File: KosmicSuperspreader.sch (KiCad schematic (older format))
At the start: 5 parts

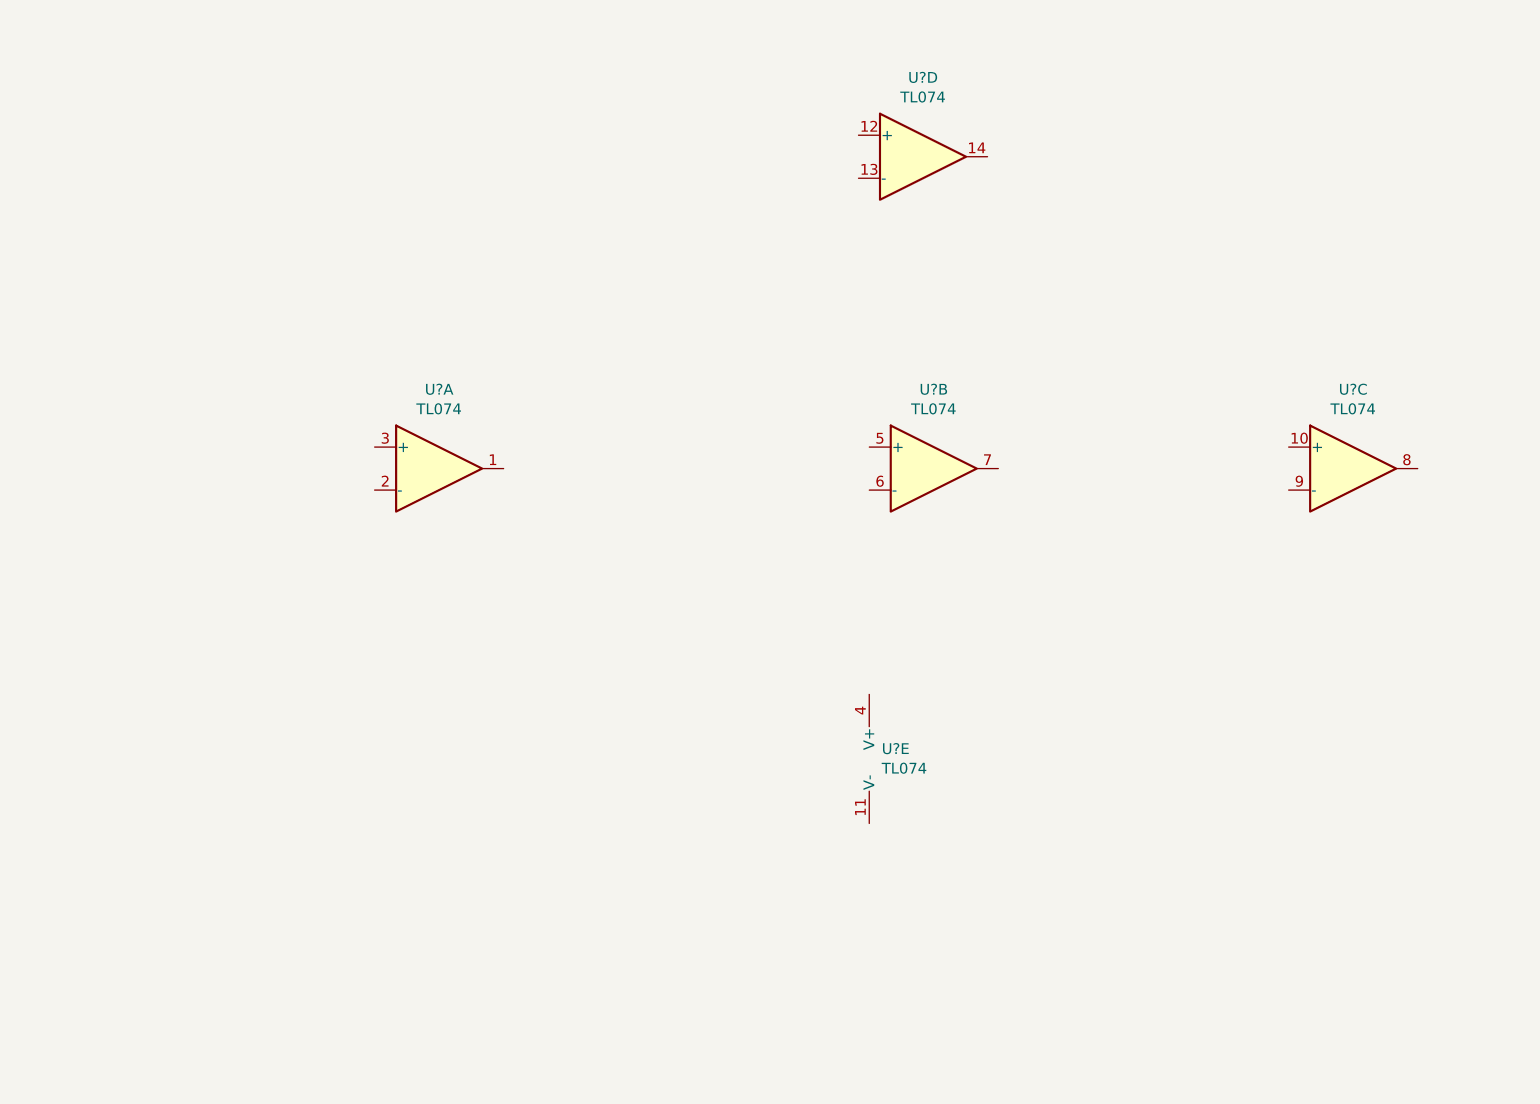
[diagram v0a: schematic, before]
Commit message: Add resistors
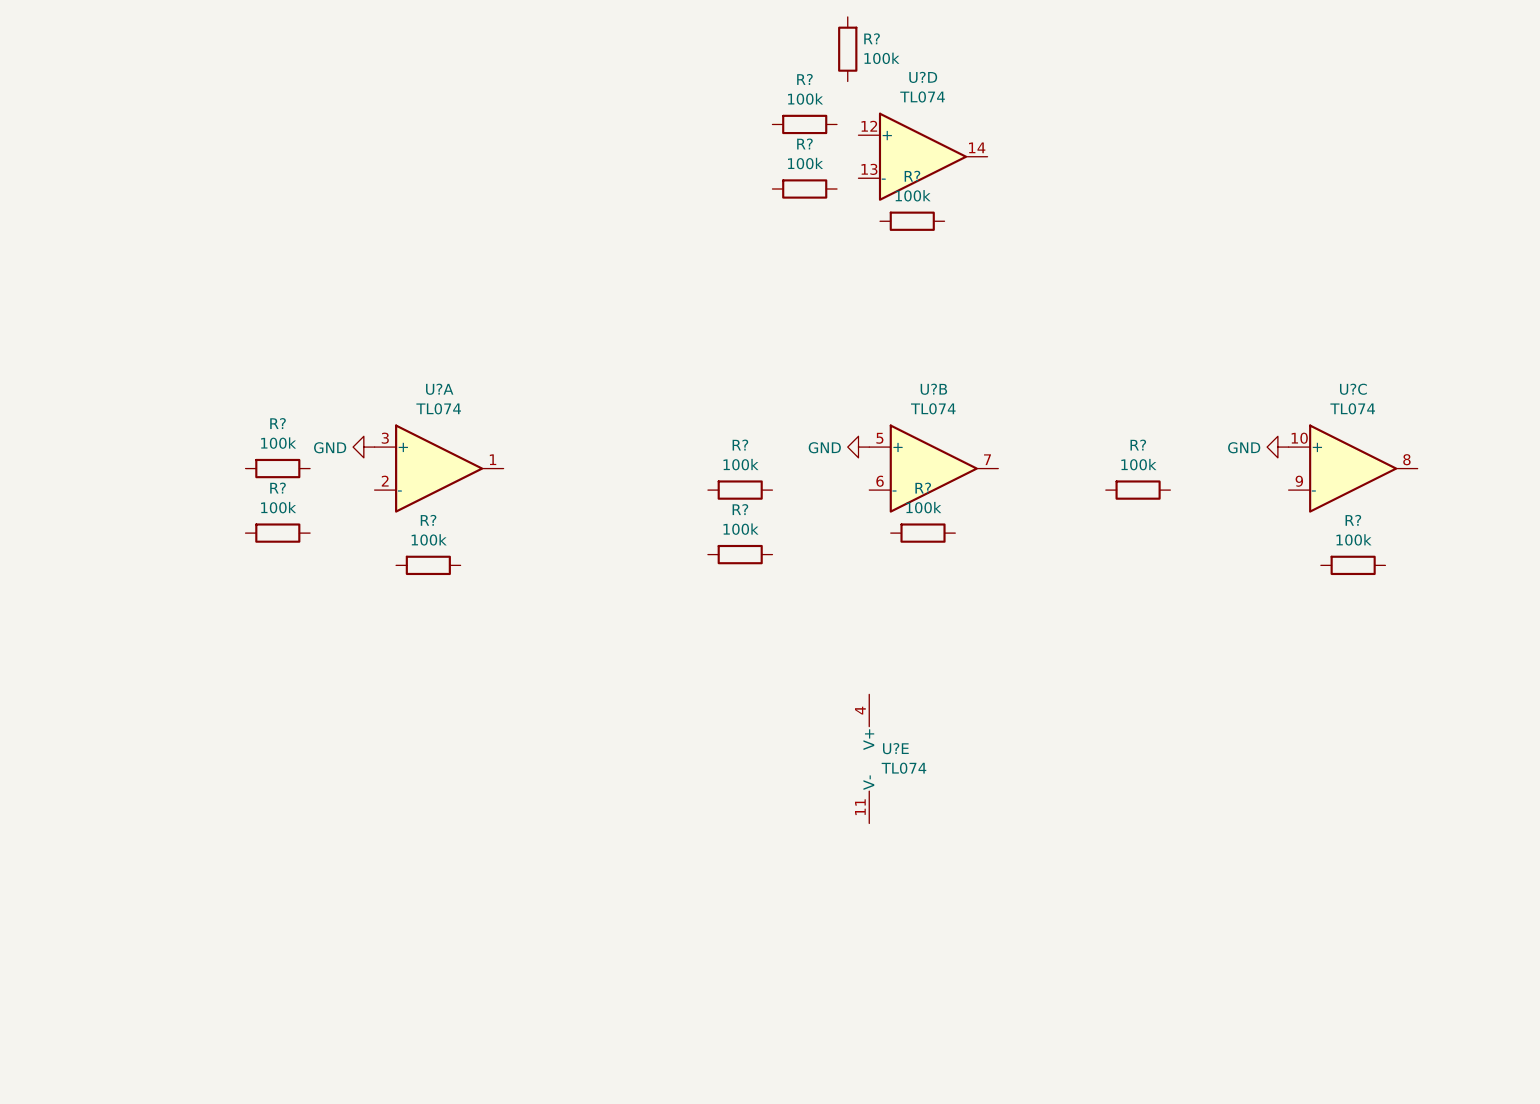
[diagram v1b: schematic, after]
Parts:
- added R? (x12): 100k, symbol Device:R
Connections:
- net GND: now reaches U?.3 (+)
- net GND: now also U?.10 (+), U?.5 (+)
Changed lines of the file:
@@
 	1    0    0    -1
 $EndComp
+$Comp
+L power:GND #PWR?
+U 1 1 60B1F41E
+P 2700 3900
+F 0 "#PWR?" H 2700 3650 50  0001 C CNN
+F 1 "GND" V 2705 3772 50  0000 R CNN
+F 2 "" H 2700 3900 50  0001 C CNN
+F 3 "" H 2700 3900 50  0001 C CNN
+	1    2700 3900
+	0    1    1    0
+$EndComp
+$Comp
+L power:GND #PWR?
+U 1 1 60B1F83E
+P 5000 3900
+F 0 "#PWR?" H 5000 3650 50  0001 C CNN
+F 1 "GND" V 5005 3772 50  0000 R CNN
+F 2 "" H 5000 3900 50  0001 C CNN
+F 3 "" H 5000 3900 50  0001 C CNN
+	1    5000 3900
+	0    1    1    0
+$EndComp
+$Comp
+L power:GND #PWR?
+U 1 1 60B1FCAA
+P 6950 3900
+F 0 "#PWR?" H 6950 3650 50  0001 C CNN
+F 1 "GND" V 6955 3772 50  0000 R CNN
+F 2 "" H 6950 3900 50  0001 C CNN
+F 3 "" H 6950 3900 50  0001 C CNN
+	1    6950 3900
+	0    1    1    0
+$EndComp
+$Comp
+L Device:R R?
+U 1 1 60B211E0
+P 5200 2850
+F 0 "R?" V 4993 2850 50  0000 C CNN
+F 1 "100k" V 5084 2850 50  0000 C CNN
+F 2 "" V 5130 2850 50  0001 C CNN
+F 3 "~" H 5200 2850 50  0001 C CNN
+F 4 "A-2248" V 5200 2850 50  0001 C CNN "Part"
+	1    5200 2850
+	0    1    1    0
+$EndComp
+$Comp
+L Device:R R?
+U 1 1 60B214C6
+P 5250 4300
+F 0 "R?" V 5043 4300 50  0000 C CNN
+F 1 "100k" V 5134 4300 50  0000 C CNN
+F 2 "" V 5180 4300 50  0001 C CNN
+F 3 "~" H 5250 4300 50  0001 C CNN
+F 4 "A-2248" V 5250 4300 50  0001 C CNN "Part"
+	1    5250 4300
+	0    1    1    0
+$EndComp
+$Comp
+L Device:R R?
+U 1 1 60B21E94
+P 4400 4100
+F 0 "R?" V 4193 4100 50  0000 C CNN
+F 1 "100k" V 4284 4100 50  0000 C CNN
+F 2 "" V 4330 4100 50  0001 C CNN
+F 3 "~" H 4400 4100 50  0001 C CNN
+F 4 "A-2248" V 4400 4100 50  0001 C CNN "Part"
+	1    4400 4100
+	0    1    1    0
+$EndComp
+$Comp
+L Device:R R?
+U 1 1 60B22499
+P 4400 4400
+F 0 "R?" V 4193 4400 50  0000 C CNN
+F 1 "100k" V 4284 4400 50  0000 C CNN
+F 2 "" V 4330 4400 50  0001 C CNN
+F 3 "~" H 4400 4400 50  0001 C CNN
+F 4 "A-2248" V 4400 4400 50  0001 C CNN "Part"
+	1    4400 4400
+	0    1    1    0
+$EndComp
+$Comp
+L Device:R R?
+U 1 1 60B2276E
+P 4700 2400
+F 0 "R?" V 4493 2400 50  0000 C CNN
+F 1 "100k" V 4584 2400 50  0000 C CNN
+F 2 "" V 4630 2400 50  0001 C CNN
+F 3 "~" H 4700 2400 50  0001 C CNN
+F 4 "A-2248" V 4700 2400 50  0001 C CNN "Part"
+	1    4700 2400
+	0    1    1    0
+$EndComp
+$Comp
+L Device:R R?
+U 1 1 60B22DB5
+P 4700 2700
+F 0 "R?" V 4493 2700 50  0000 C CNN
+F 1 "100k" V 4584 2700 50  0000 C CNN
+F 2 "" V 4630 2700 50  0001 C CNN
+F 3 "~" H 4700 2700 50  0001 C CNN
+F 4 "A-2248" V 4700 2700 50  0001 C CNN "Part"
+	1    4700 2700
+	0    1    1    0
+$EndComp
+$Comp
+L Device:R R?
+U 1 1 60B23C3D
+P 4900 2050
+F 0 "R?" H 4830 2004 50  0000 R CNN
+F 1 "100k" H 4830 2095 50  0000 R CNN
+F 2 "" V 4830 2050 50  0001 C CNN
+F 3 "~" H 4900 2050 50  0001 C CNN
+F 4 "A-2248" V 4900 2050 50  0001 C CNN "Part"
+	1    4900 2050
+	-1   0    0    1
+$EndComp
+$Comp
+L Device:R R?
+U 1 1 60B242ED
+P 6250 4100
+F 0 "R?" V 6043 4100 50  0000 C CNN
+F 1 "100k" V 6134 4100 50  0000 C CNN
+F 2 "" V 6180 4100 50  0001 C CNN
+F 3 "~" H 6250 4100 50  0001 C CNN
+F 4 "A-2248" V 6250 4100 50  0001 C CNN "Part"
+	1    6250 4100
+	0    1    1    0
+$EndComp
+$Comp
+L Device:R R?
+U 1 1 60B24980
+P 7250 4450
+F 0 "R?" V 7043 4450 50  0000 C CNN
+F 1 "100k" V 7134 4450 50  0000 C CNN
+F 2 "" V 7180 4450 50  0001 C CNN
+F 3 "~" H 7250 4450 50  0001 C CNN
+F 4 "A-2248" V 7250 4450 50  0001 C CNN "Part"
+	1    7250 4450
+	0    1    1    0
+$EndComp
+$Comp
+L Device:R R?
+U 1 1 60B24D1D
+P 2950 4450
+F 0 "R?" V 2743 4450 50  0000 C CNN
+F 1 "100k" V 2834 4450 50  0000 C CNN
+F 2 "" V 2880 4450 50  0001 C CNN
+F 3 "~" H 2950 4450 50  0001 C CNN
+F 4 "A-2248" V 2950 4450 50  0001 C CNN "Part"
+	1    2950 4450
+	0    1    1    0
+$EndComp
+$Comp
+L Device:R R?
+U 1 1 60B25284
+P 2250 4300
+F 0 "R?" V 2043 4300 50  0000 C CNN
+F 1 "100k" V 2134 4300 50  0000 C CNN
+F 2 "" V 2180 4300 50  0001 C CNN
+F 3 "~" H 2250 4300 50  0001 C CNN
+F 4 "A-2248" V 2250 4300 50  0001 C CNN "Part"
+	1    2250 4300
+	0    1    1    0
+$EndComp
+$Comp
+L Device:R R?
+U 1 1 60B25ADF
+P 2250 4000
+F 0 "R?" V 2043 4000 50  0000 C CNN
+F 1 "100k" V 2134 4000 50  0000 C CNN
+F 2 "" V 2180 4000 50  0001 C CNN
+F 3 "~" H 2250 4000 50  0001 C CNN
+F 4 "A-2248" V 2250 4000 50  0001 C CNN "Part"
+	1    2250 4000
+	0    1    1    0
+$EndComp
 $EndSCHEMATC

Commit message: wires
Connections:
- net GND: now also R?.2
- net at U?.1: now also R?.1
- net at U?.2 (-): now also R?.1, R?.1, R?.2
- net at U?.6 (-): now also R?.1, R?.1, R?.2
- net at U?.7: now also R?.1, R?.2
- net at U?.8: now also R?.1
- net at U?.9 (-): now also R?.1, R?.2
- net at U?.12 (+): now also R?.1, R?.1
- net at U?.13 (-): now also R?.1, R?.2
- net at U?.14: now also R?.1
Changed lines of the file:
@@
 	0    1    1    0
 $EndComp
+Wire Wire Line
+	2400 4000 2400 4100
+Wire Wire Line
+	2700 4100 2400 4100
+Connection ~ 2400 4100
+Wire Wire Line
+	2400 4100 2400 4300
+Wire Wire Line
+	2800 4450 2700 4450
+Wire Wire Line
+	2700 4450 2700 4100
+Connection ~ 2700 4100
+Wire Wire Line
+	3100 4450 3300 4450
+Wire Wire Line
+	3300 4450 3300 4000
+Wire Wire Line
+	4550 4100 4550 4400
+Wire Wire Line
+	5000 4100 4550 4100
+Connection ~ 4550 4100
+Wire Wire Line
+	5100 4300 5000 4300
+Wire Wire Line
+	5000 4300 5000 4100
+Connection ~ 5000 4100
+Wire Wire Line
+	5400 4300 5600 4300
+Wire Wire Line
+	5600 4300 5600 4100
+Wire Wire Line
+	6400 4100 6950 4100
+Wire Wire Line
+	6100 4100 5600 4100
+Connection ~ 5600 4100
+Wire Wire Line
+	5600 4100 5600 4000
+Wire Wire Line
+	7100 4450 6950 4450
+Wire Wire Line
+	6950 4450 6950 4100
+Connection ~ 6950 4100
+Wire Wire Line
+	7550 4000 7550 4450
+Wire Wire Line
+	7550 4450 7400 4450
+Wire Wire Line
+	4850 2700 4950 2700
+Wire Wire Line
+	4950 2700 4950 2650
+Wire Wire Line
+	4850 2400 4900 2400
+Wire Wire Line
+	4950 2400 4950 2450
+Wire Wire Line
+	5350 2850 5550 2850
+Wire Wire Line
+	5550 2850 5550 2550
+Wire Wire Line
+	5050 2850 4950 2850
+Wire Wire Line
+	4950 2850 4950 2700
+Connection ~ 4950 2700
+Wire Wire Line
+	4900 2200 4900 2400
+Connection ~ 4900 2400
+Wire Wire Line
+	4900 2400 4950 2400
+$Comp
+L power:GND #PWR?
+U 1 1 60B2A62B
+P 5400 1900
+F 0 "#PWR?" H 5400 1650 50  0001 C CNN
+F 1 "GND" H 5405 1727 50  0000 C CNN
+F 2 "" H 5400 1900 50  0001 C CNN
+F 3 "" H 5400 1900 50  0001 C CNN
+	1    5400 1900
+	1    0    0    -1
+$EndComp
+Wire Wire Line
+	4900 1900 5400 1900
 $EndSCHEMATC

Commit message: Jacks
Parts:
- added J? (x5): AudioJack2_Ground_Switch, symbol Connector:AudioJack2_Ground_Switch
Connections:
- net GND: now also J?.G, J?.G, J?.G, J?.G, J?.G
- net at R?.1, U?.1: now also R?.2, R?.2
- net at R?.2: now also R?.2
- no-connect marks 0 -> 15
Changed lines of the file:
@@
 	3100 4450 3300 4450
-Wire Wire Line
-	3300 4450 3300 4000
 Wire Wire Line
 	4550 4100 4550 4400
@@
 Wire Wire Line
 	4900 1900 5400 1900
+Wire Wire Line
+	3300 4100 3400 4100
+Wire Wire Line
+	3300 4000 3300 4100
+Connection ~ 3300 4100
+Wire Wire Line
+	3300 4100 3300 4450
+Wire Wire Line
+	3400 4100 3400 2700
+Wire Wire Line
+	3400 2700 4550 2700
+Connection ~ 3400 4100
+Wire Wire Line
+	3400 4100 4250 4100
+Wire Wire Line
+	4250 4400 4000 4400
+Wire Wire Line
+	4000 4400 4000 2400
+Wire Wire Line
+	4000 2400 4550 2400
+$Comp
+L Connector:AudioJack2_Ground_Switch J?
+U 1 1 60B2E747
+P 2200 6350
+F 0 "J?" H 2232 6775 50  0000 C CNN
+F 1 "AudioJack2_Ground_Switch" H 2232 6684 50  0000 C CNN
+F 2 "" H 2200 6550 50  0001 C CNN
+F 3 "~" H 2200 6550 50  0001 C CNN
+F 4 "A-1121" H 2200 6350 50  0001 C CNN "Part"
+	1    2200 6350
+	1    0    0    -1
+$EndComp
+NoConn ~ 2400 6450
+NoConn ~ 2400 6250
+NoConn ~ 2400 6150
+$Comp
+L power:GND #PWR?
+U 1 1 60B30BB2
+P 2200 6650
+F 0 "#PWR?" H 2200 6400 50  0001 C CNN
+F 1 "GND" H 2205 6477 50  0000 C CNN
+F 2 "" H 2200 6650 50  0001 C CNN
+F 3 "" H 2200 6650 50  0001 C CNN
+	1    2200 6650
+	1    0    0    -1
+$EndComp
+$Comp
+L Connector:AudioJack2_Ground_Switch J?
+U 1 1 60B31450
+P 2900 6350
+F 0 "J?" H 2932 6775 50  0000 C CNN
+F 1 "AudioJack2_Ground_Switch" H 2932 6684 50  0000 C CNN
+F 2 "" H 2900 6550 50  0001 C CNN
+F 3 "~" H 2900 6550 50  0001 C CNN
+F 4 "A-1121" H 2900 6350 50  0001 C CNN "Part"
+	1    2900 6350
+	1    0    0    -1
+$EndComp
+NoConn ~ 3100 6450
+NoConn ~ 3100 6250
+NoConn ~ 3100 6150
+$Comp
+L power:GND #PWR?
+U 1 1 60B31769
+P 2900 6650
+F 0 "#PWR?" H 2900 6400 50  0001 C CNN
+F 1 "GND" H 2905 6477 50  0000 C CNN
+F 2 "" H 2900 6650 50  0001 C CNN
+F 3 "" H 2900 6650 50  0001 C CNN
+	1    2900 6650
+	1    0    0    -1
+$EndComp
+$Comp
+L Connector:AudioJack2_Ground_Switch J?
+U 1 1 60B33779
+P 3550 6350
+F 0 "J?" H 3582 6775 50  0000 C CNN
+F 1 "AudioJack2_Ground_Switch" H 3582 6684 50  0000 C CNN
+F 2 "" H 3550 6550 50  0001 C CNN
+F 3 "~" H 3550 6550 50  0001 C CNN
+F 4 "A-1121" H 3550 6350 50  0001 C CNN "Part"
+	1    3550 6350
+	1    0    0    -1
+$EndComp
+NoConn ~ 3750 6450
+NoConn ~ 3750 6250
+NoConn ~ 3750 6150
+$Comp
+L power:GND #PWR?
+U 1 1 60B33AC2
+P 3550 6650
+F 0 "#PWR?" H 3550 6400 50  0001 C CNN
+F 1 "GND" H 3555 6477 50  0000 C CNN
+F 2 "" H 3550 6650 50  0001 C CNN
+F 3 "" H 3550 6650 50  0001 C CNN
+	1    3550 6650
+	1    0    0    -1
+$EndComp
+$Comp
+L Connector:AudioJack2_Ground_Switch J?
+U 1 1 60B33ACD
+P 4250 6350
+F 0 "J?" H 4282 6775 50  0000 C CNN
+F 1 "AudioJack2_Ground_Switch" H 4282 6684 50  0000 C CNN
+F 2 "" H 4250 6550 50  0001 C CNN
+F 3 "~" H 4250 6550 50  0001 C CNN
+F 4 "A-1121" H 4250 6350 50  0001 C CNN "Part"
+	1    4250 6350
+	1    0    0    -1
+$EndComp
+NoConn ~ 4450 6450
+NoConn ~ 4450 6250
+NoConn ~ 4450 6150
+$Comp
+L power:GND #PWR?
+U 1 1 60B33ADA
+P 4250 6650
+F 0 "#PWR?" H 4250 6400 50  0001 C CNN
+F 1 "GND" H 4255 6477 50  0000 C CNN
+F 2 "" H 4250 6650 50  0001 C CNN
+F 3 "" H 4250 6650 50  0001 C CNN
+	1    4250 6650
+	1    0    0    -1
+$EndComp
+$Comp
+L Connector:AudioJack2_Ground_Switch J?
+U 1 1 60B3629C
+P 1600 6350
+F 0 "J?" H 1632 6775 50  0000 C CNN
+F 1 "AudioJack2_Ground_Switch" H 1632 6684 50  0000 C CNN
+F 2 "" H 1600 6550 50  0001 C CNN
+F 3 "~" H 1600 6550 50  0001 C CNN
+F 4 "A-1121" H 1600 6350 50  0001 C CNN "Part"
+	1    1600 6350
+	1    0    0    -1
+$EndComp
+NoConn ~ 1800 6450
+NoConn ~ 1800 6250
+NoConn ~ 1800 6150
+$Comp
+L power:GND #PWR?
+U 1 1 60B36645
+P 1600 6650
+F 0 "#PWR?" H 1600 6400 50  0001 C CNN
+F 1 "GND" H 1605 6477 50  0000 C CNN
+F 2 "" H 1600 6650 50  0001 C CNN
+F 3 "" H 1600 6650 50  0001 C CNN
+	1    1600 6650
+	1    0    0    -1
+$EndComp
 $EndSCHEMATC

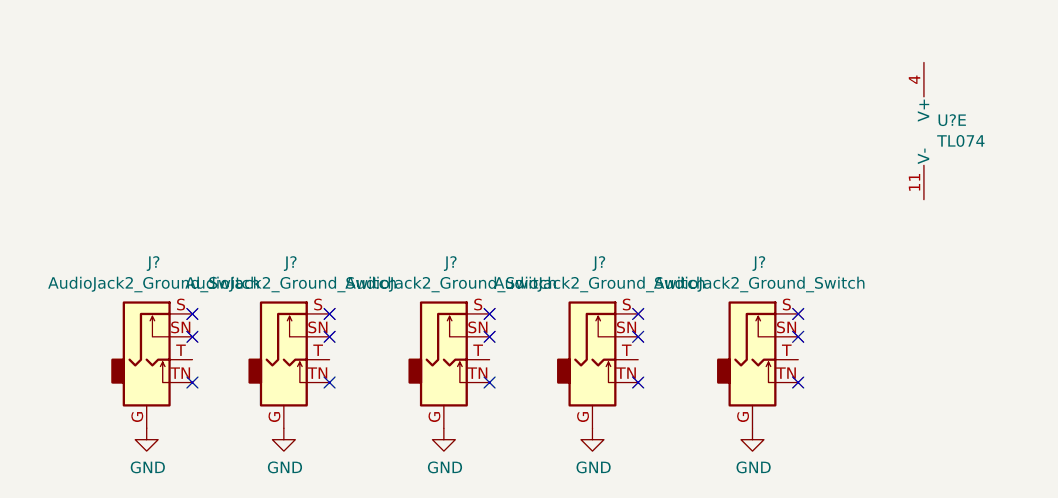
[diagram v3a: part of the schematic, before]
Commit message: Jack labels
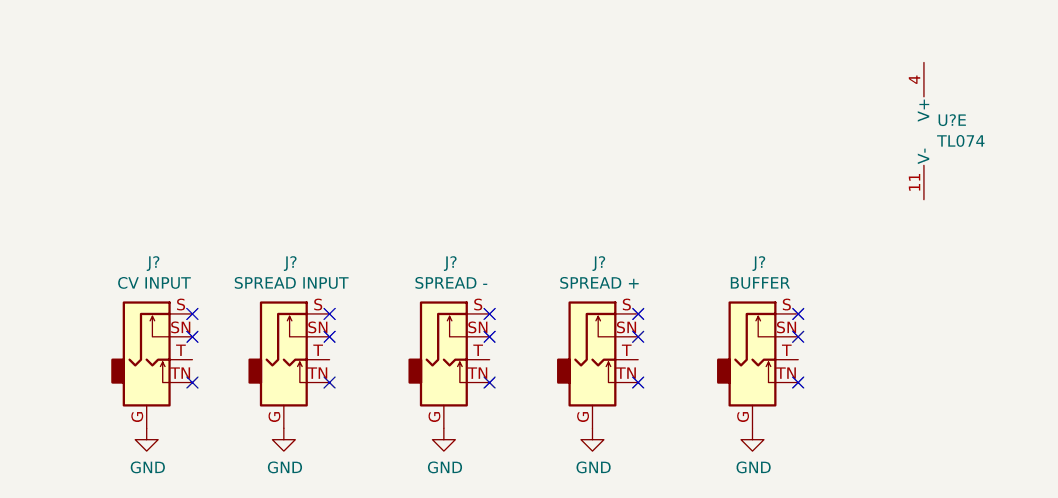
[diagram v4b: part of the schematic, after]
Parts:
- J?: value AudioJack2_Ground_Switch -> SPREAD INPUT
- J?: value AudioJack2_Ground_Switch -> SPREAD -
- J?: value AudioJack2_Ground_Switch -> SPREAD +
- J?: value AudioJack2_Ground_Switch -> BUFFER
- J?: value AudioJack2_Ground_Switch -> CV INPUT
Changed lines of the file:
@@
 P 2200 6350
 F 0 "J?" H 2232 6775 50  0000 C CNN
-F 1 "AudioJack2_Ground_Switch" H 2232 6684 50  0000 C CNN
+F 1 "SPREAD INPUT" H 2232 6684 50  0000 C CNN
 F 2 "" H 2200 6550 50  0001 C CNN
 F 3 "~" H 2200 6550 50  0001 C CNN
@@
 P 2900 6350
 F 0 "J?" H 2932 6775 50  0000 C CNN
-F 1 "AudioJack2_Ground_Switch" H 2932 6684 50  0000 C CNN
+F 1 "SPREAD -" H 2932 6684 50  0000 C CNN
 F 2 "" H 2900 6550 50  0001 C CNN
 F 3 "~" H 2900 6550 50  0001 C CNN
@@
 P 3550 6350
 F 0 "J?" H 3582 6775 50  0000 C CNN
-F 1 "AudioJack2_Ground_Switch" H 3582 6684 50  0000 C CNN
+F 1 "SPREAD +" H 3582 6684 50  0000 C CNN
 F 2 "" H 3550 6550 50  0001 C CNN
 F 3 "~" H 3550 6550 50  0001 C CNN
@@
 P 4250 6350
 F 0 "J?" H 4282 6775 50  0000 C CNN
-F 1 "AudioJack2_Ground_Switch" H 4282 6684 50  0000 C CNN
+F 1 "BUFFER" H 4282 6684 50  0000 C CNN
 F 2 "" H 4250 6550 50  0001 C CNN
 F 3 "~" H 4250 6550 50  0001 C CNN
@@
 P 1600 6350
 F 0 "J?" H 1632 6775 50  0000 C CNN
-F 1 "AudioJack2_Ground_Switch" H 1632 6684 50  0000 C CNN
+F 1 "CV INPUT" H 1632 6684 50  0000 C CNN
 F 2 "" H 1600 6550 50  0001 C CNN
 F 3 "~" H 1600 6550 50  0001 C CNN
